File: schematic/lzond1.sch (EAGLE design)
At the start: 16 parts, among them IC1 786TV

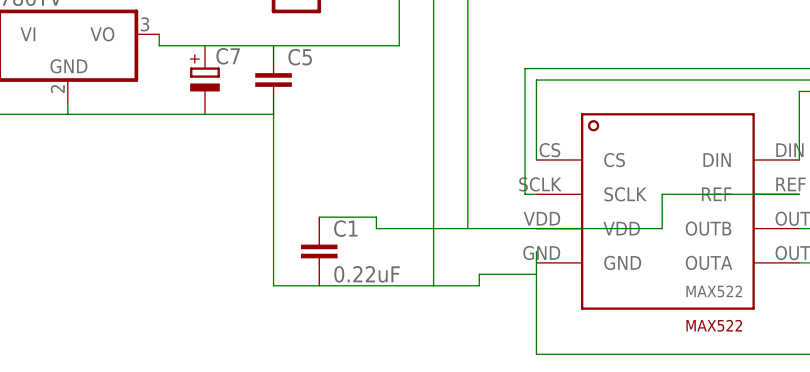
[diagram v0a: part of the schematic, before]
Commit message: Fixed bug in mix definition
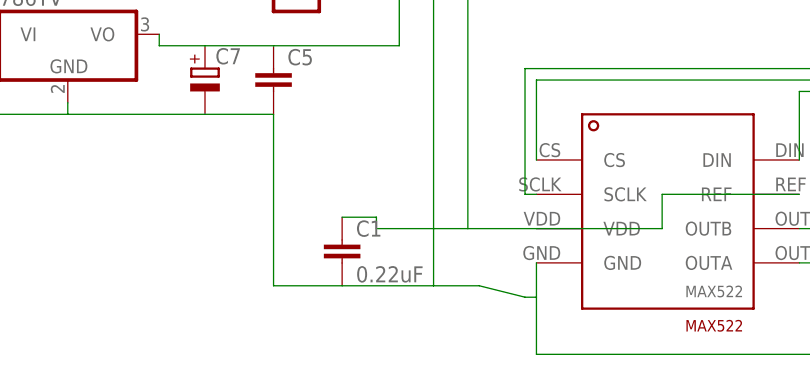
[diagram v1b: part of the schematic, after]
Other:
- moved on the sheet: C1
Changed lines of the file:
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@@
 <setting verticaltext="up"/>
 </settings>
-<grid distance="1.27" unitdist="mm" unit="mm" style="lines" multiple="1" display="yes" altdistance="0.254" altunitdist="mm" altunit="mm"/>
+<grid distance="0.1" unitdist="inch" unit="inch" style="lines" multiple="1" display="no" altdistance="0.01" altunitdist="inch" altunit="inch"/>
 <layers>
 <layer number="1" name="Top" color="4" fill="1" visible="no" active="no"/>
@@
 <instance part="S1" gate="1" x="66.04" y="80.01" rot="R270"/>
 <instance part="U$2" gate="G$1" x="35.56" y="-8.89"/>
-<instance part="C1" gate="G$1" x="-7.62" y="-12.7"/>
+<instance part="C1" gate="G$1" x="-5.08" y="-12.7"/>
 <instance part="C2" gate="G$1" x="69.85" y="-15.24"/>
 <instance part="C3" gate="G$1" x="69.85" y="-3.81"/>
@@
 <pinref part="U$2" gate="G$1" pin="VDD"/>
 <pinref part="C1" gate="G$1" pin="1"/>
-<wire x1="-7.62" y1="-10.16" x2="-1.27" y2="-10.16" width="0.1524" layer="91"/>
+<wire x1="-5.08" y1="-10.16" x2="-1.27" y2="-10.16" width="0.1524" layer="91"/>
 <wire x1="-1.27" y1="-10.16" x2="-1.27" y2="-11.43" width="0.1524" layer="91"/>
 <wire x1="-1.27" y1="-11.43" x2="8.89" y2="-11.43" width="0.1524" layer="91"/>
@@
 <wire x1="-12.7" y1="1.27" x2="-12.7" y2="-17.78" width="0.1524" layer="91"/>
 <pinref part="U$2" gate="G$1" pin="GND"/>
-<wire x1="16.51" y1="-13.97" x2="16.51" y2="-15.24" width="0.1524" layer="91"/>
-<wire x1="10.16" y1="-16.51" x2="16.51" y2="-16.51" width="0.1524" layer="91"/>
-<wire x1="16.51" y1="-16.51" x2="16.51" y2="-15.24" width="0.1524" layer="91"/>
+<wire x1="15.24" y1="-19.05" x2="16.51" y2="-19.05" width="0.1524" layer="91"/>
+<wire x1="16.51" y1="-19.05" x2="16.51" y2="-15.24" width="0.1524" layer="91"/>
 <pinref part="C1" gate="G$1" pin="2"/>
-<wire x1="-7.62" y1="-17.78" x2="5.08" y2="-17.78" width="0.1524" layer="91"/>
+<wire x1="-5.08" y1="-17.78" x2="5.08" y2="-17.78" width="0.1524" layer="91"/>
 <wire x1="5.08" y1="-17.78" x2="10.16" y2="-17.78" width="0.1524" layer="91"/>
-<wire x1="10.16" y1="-17.78" x2="10.16" y2="-16.51" width="0.1524" layer="91"/>
+<wire x1="10.16" y1="-17.78" x2="15.24" y2="-19.05" width="0.1524" layer="91"/>
 <pinref part="C3" gate="G$1" pin="2"/>
 <wire x1="69.85" y1="-8.89" x2="76.2" y2="-8.89" width="0.1524" layer="91"/>
@@
 <wire x1="64.77" y1="-20.32" x2="64.77" y2="-25.4" width="0.1524" layer="91"/>
 <wire x1="64.77" y1="-25.4" x2="16.51" y2="-25.4" width="0.1524" layer="91"/>
-<wire x1="16.51" y1="-25.4" x2="16.51" y2="-16.51" width="0.1524" layer="91"/>
+<wire x1="16.51" y1="-25.4" x2="16.51" y2="-19.05" width="0.1524" layer="91"/>
 <wire x1="5.08" y1="-17.78" x2="5.08" y2="17.78" width="0.1524" layer="91"/>
 <pinref part="SV3" gate="1" pin="20"/>
@@
 <pinref part="SV5" gate="1" pin="18"/>
 <wire x1="139.7" y1="19.05" x2="140.97" y2="19.05" width="0.1524" layer="91"/>
-<wire x1="-12.7" y1="-17.78" x2="-7.62" y2="-17.78" width="0.1524" layer="91"/>
+<wire x1="-12.7" y1="-17.78" x2="-5.08" y2="-17.78" width="0.1524" layer="91"/>
 <pinref part="LED1" gate="G$1" pin="C"/>
 <wire x1="101.6" y1="15.24" x2="101.6" y2="7.62" width="0.1524" layer="91"/>
